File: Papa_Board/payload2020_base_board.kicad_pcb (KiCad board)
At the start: 4 copper layers, 82 x 82 mm, 101 parts, among them J1 1862, J10 1862, J11 Conn_01x05, J2 Conn_01x05, J3 Conn_01x05_Female, J4 Conn_01x05, J5 M80-5000642, J6 M80-5000642, J7 1862, J8 693072010801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

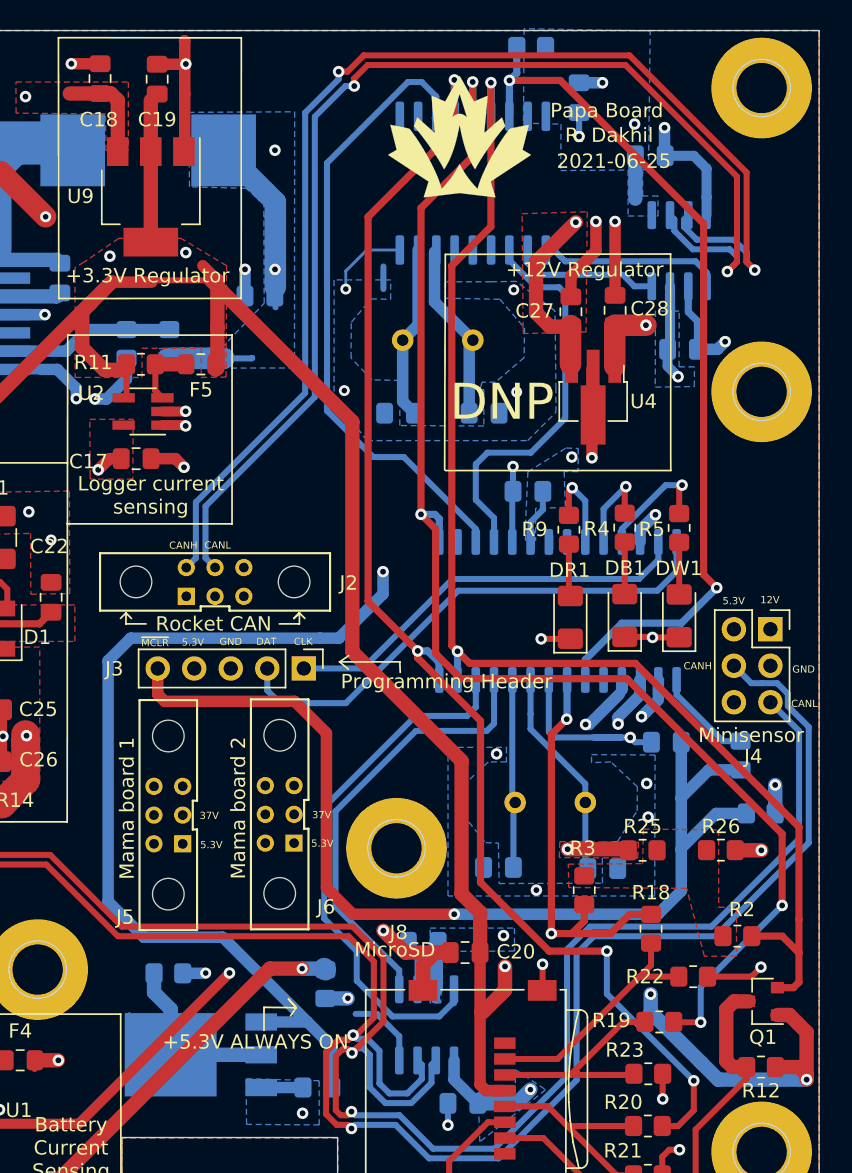
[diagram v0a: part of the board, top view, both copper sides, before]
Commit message: Move 3V3 line and rocket CAN traces
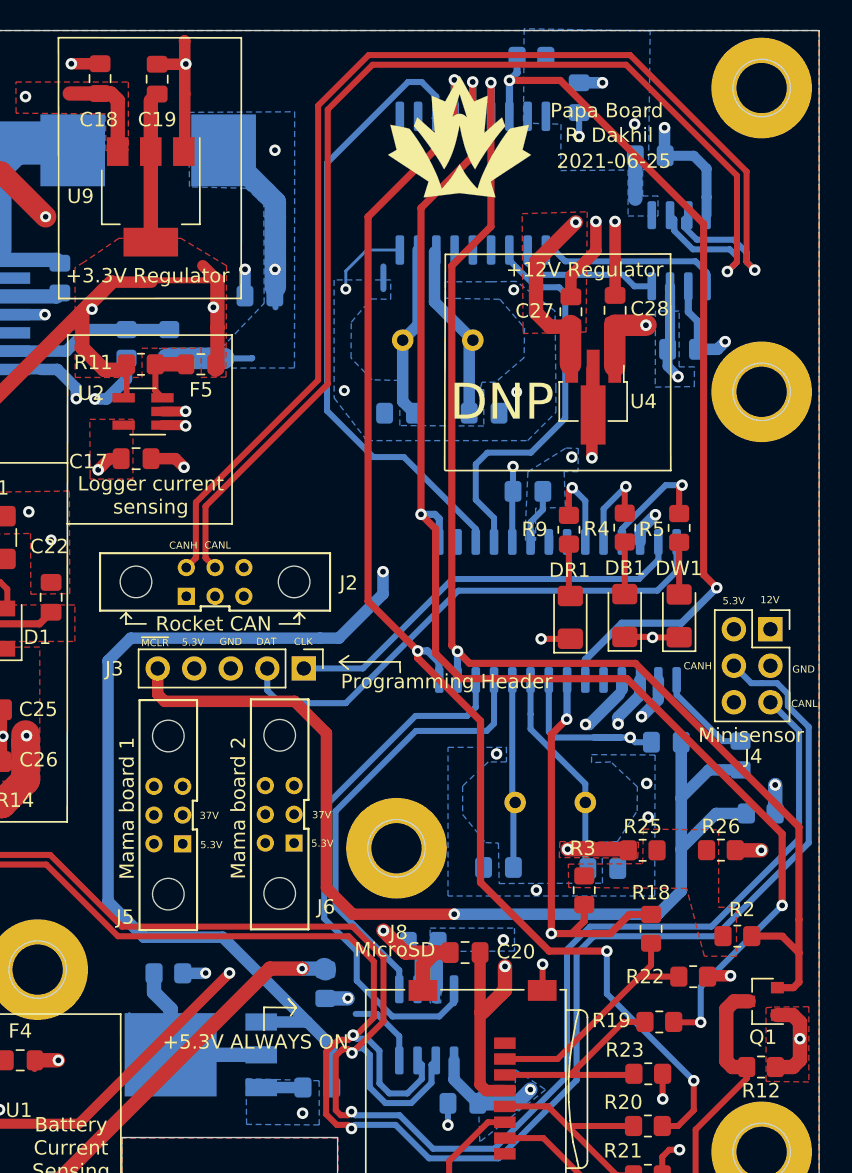
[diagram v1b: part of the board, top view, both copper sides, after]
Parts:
- moved R24 0.69 mm to (97.5, 69.1)
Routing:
- net +3V3: track 176.1 -> 189.5 mm, vias 5 -> 4
- net GND: track 182.9 -> 180.6 mm
- net /MCU and CAN controllers/CS_1: track 61.6 -> 60.8 mm
- net /CANL_ROCKET: track 83.7 -> 83.2 mm, vias 2 -> 1
- net /CANH_ROCKET: track 85.6 -> 85.1 mm, vias 2 -> 1

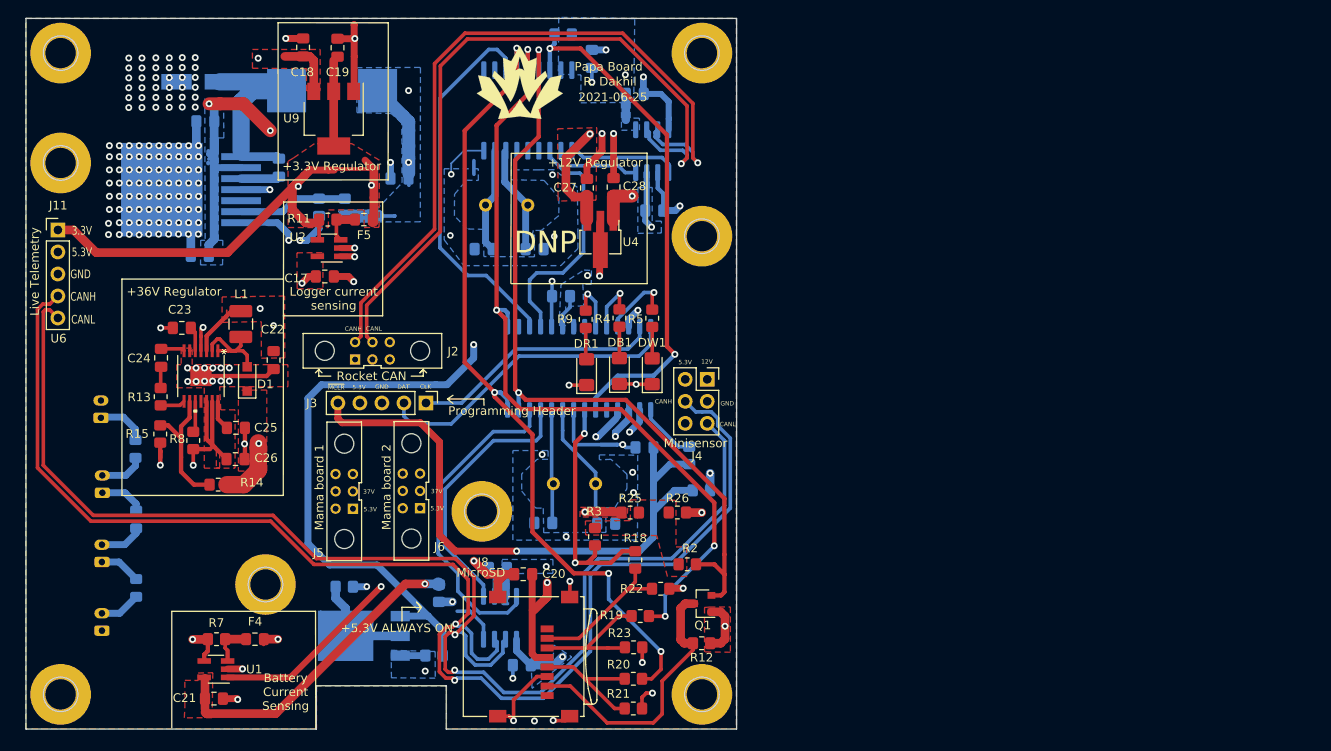
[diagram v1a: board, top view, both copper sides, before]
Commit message: Address Lance's comments, change microSD voltage divider resistor values (in-stock resistors)
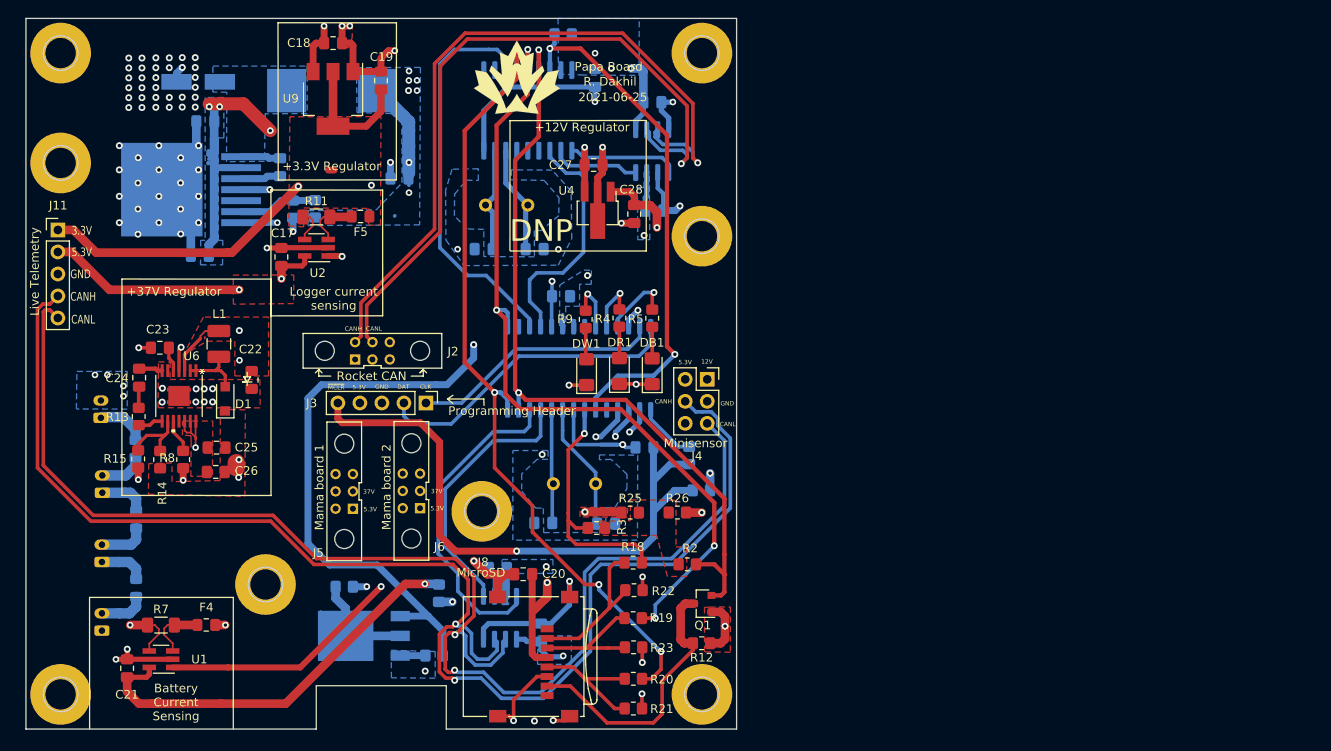
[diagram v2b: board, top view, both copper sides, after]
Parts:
- C7: value 56uF -> 100uF
- R11, R7: footprint Resistor_SMD:R_0805_2012Metric_Pad1.20x1.40mm_HandSolder -> Resistor_SMD:R_1206_3216Metric_Pad1.30x1.75mm_HandSolder
- R18, R19, R20: value 34kR -> 68kR
- R21, R22, R23: value 66kR -> 132kR
- moved C21 10.6 mm to (47.2, 142.3), turned to 270 degrees
- moved R14 7.30 mm to (51.0, 118.2), turned to 90 degrees
- moved R7 6.61 mm to (51.1, 137.3)
- moved U1 6.44 mm to (51.1, 141.3)
- moved C19 6.29 mm to (76.5, 74.5)
- moved F4 5.85 mm to (56.4, 137.3)
- moved C17 5.50 mm to (65.0, 94.8), turned to 270 degrees
- moved C14 4.36 mm to (95.0, 138.2), turned to 90 degrees
- moved C28 3.92 mm to (105.7, 89.9), turned to 270 degrees
- moved R15 3.84 mm to (48.5, 118.1)
- moved C18 3.50 mm to (71.0, 70.2), turned to 180 degrees
- moved R16 3.44 mm to (68.9, 89.3)
- moved D1 3.41 mm to (58.6, 111.2)
- moved C24 3.41 mm to (48.6, 108.8)
- moved R13 3.41 mm to (48.6, 113.2)
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- renumbered DW1 to DB1, DB1 to DR1, DR1 to DW1
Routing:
- net /+5.3V: track 72.8 -> 98.4 mm, vias 6 -> 12
- net Net-(C6-Pad1): track 25.4 -> 7.40 mm
- net +3V3: track 189.5 -> 172.6 mm
- net /+37V: track 11.5 -> 0.95 mm
- net Net-(R14-Pad2): track 15.5 -> 7.99 mm
- net GND: track 180.6 -> 173.5 mm, vias 168 -> 94
- net BATT_CURR_AMP: track 67.1 -> 73.0 mm
- net +BATT: track 105.4 -> 99.8 mm, vias 7 -> 12
- net /PWR_EN: track 81.4 -> 86.8 mm
- net Net-(R16-Pad2): track 12.6 -> 9.09 mm
- net Net-(D1-Pad2): track 11.5 -> 8.27 mm
- net /MCU and CAN controllers/CAN_INT: track 43.8 -> 46.1 mm
- net Net-(F4-Pad2): track 5.04 -> 7.06 mm
- net Net-(F5-Pad2): track 4.68 -> 6.41 mm
- net /5V3_ALWAYS_ON: track 33.4 -> 31.7 mm, vias 10 -> 11
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- added copper zone on B.Cu, net Net-(C6-Pad1)
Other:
- board text added: "+37V Regulator"
- board text removed: "+36V Regulator"

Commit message: Clean up via placement, SPI lines, polygons
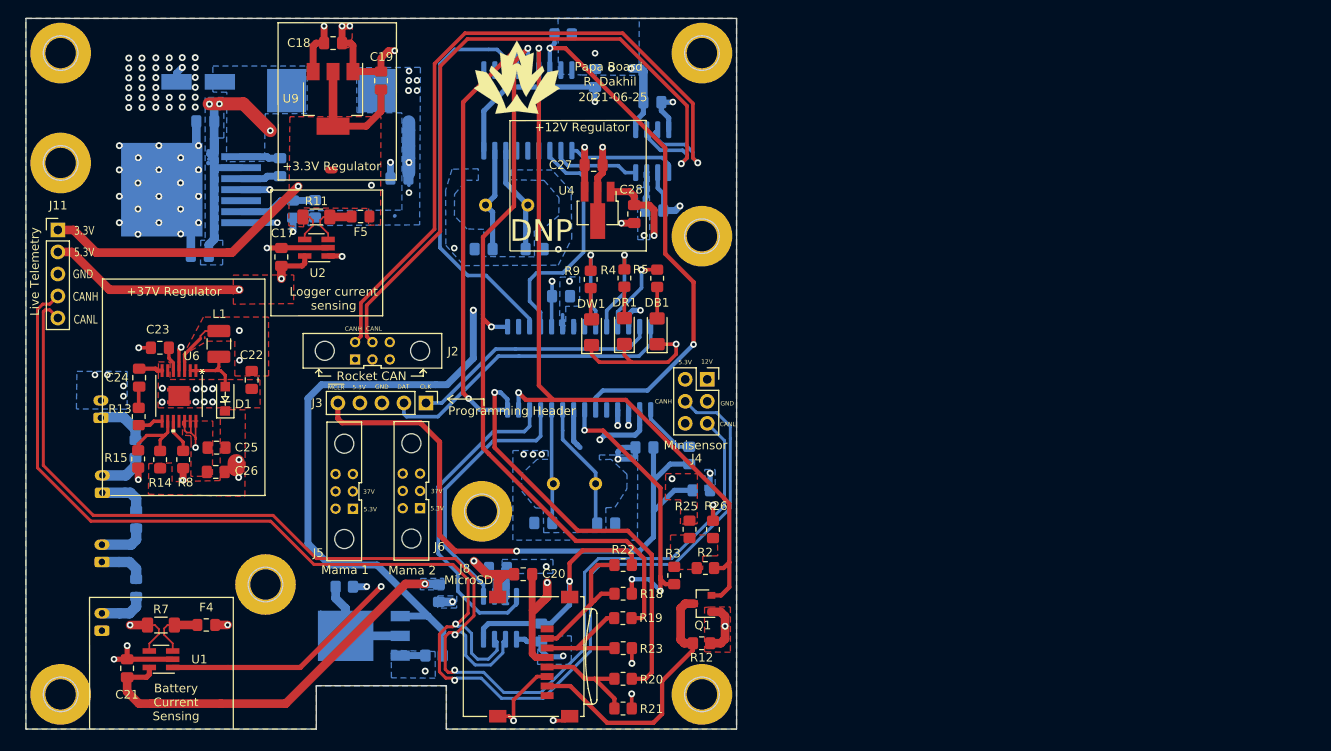
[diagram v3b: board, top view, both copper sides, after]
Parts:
- moved R3 10.5 mm to (110.4, 131.6), turned to 270 degrees
- moved R25 7.11 mm to (112.1, 126.3), turned to 270 degrees
- moved DB1 4.65 mm to (108.4, 103.4)
- moved DR1 4.65 mm to (104.6, 103.4)
- moved DW1 4.65 mm to (100.8, 103.5)
- moved R4 4.65 mm to (104.6, 97.3)
- moved R5 4.65 mm to (108.4, 97.3)
- moved R9 4.65 mm to (100.7, 97.4)
- moved R26 4.55 mm to (114.8, 126.3), turned to 90 degrees
- moved R18 3.77 mm to (104.5, 133.7)
- moved R22 3.16 mm to (104.5, 130.4)
- moved R2 2.14 mm to (114.0, 130.7)
- moved R23 1.20 mm to (104.5, 140.0)
- moved R19 1.19 mm to (104.4, 136.5)
- moved R20 1.19 mm to (104.5, 143.5)
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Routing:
- net GND: track 173.5 -> 195.5 mm
- net /+5.3V: track 98.4 -> 89.1 mm
- net /Logger board/MOSI: track 94.1 -> 86.5 mm, vias 4 -> 2
- net /Logger board/SCK: track 93.2 -> 100.2 mm, vias 4 -> 3
- net Net-(R4-Pad1): track 6.41 -> 10.8 mm
- net Net-(R9-Pad1): track 6.17 -> 10.3 mm
- net MAMA_PWR_EN: track 88.1 -> 91.8 mm
- net Net-(J8-Pad5): track 15.7 -> 12.7 mm
- net /Logger board/CS: track 31.0 -> 33.2 mm, vias 1 -> 3
- net Net-(J8-Pad3): track 15.7 -> 13.5 mm
- net 3V3_CURR_AMP: track 60.6 -> 58.7 mm
- net Net-(J8-Pad2): track 18.4 -> 16.7 mm
- net BATT_CURR_AMP: track 73.0 -> 71.4 mm
- net /MCU and CAN controllers/CS_1: track 60.8 -> 62.2 mm
- net /PWR_EN: track 86.8 -> 85.6 mm
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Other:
- net class Default: clearance 0.1524 -> 0.2032
- net class net removed
- rule trace_clearance: 0.1524 -> 0.2032
- board text added: "Mama 1"
- board text added: "Mama 2"
- board text removed: "Mama board 1"
- board text removed: "Mama board 2"

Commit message: Update D2 values and part number, update 10u capacitors' footprint
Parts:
- C22, C25, C26: footprint Capacitor_SMD:C_0805_2012Metric_Pad1.18x1.45mm_HandSolder -> Capacitor_SMD:C_1206_3216Metric_Pad1.33x1.80mm_HandSolder
- D2: value 500mV 2A -> 450mV 2A
- moved C22 0.67 mm to (61.6, 108.4)
- moved C26 0.39 mm to (57.7, 119.3)
- moved C25 0.30 mm to (57.8, 116.7)
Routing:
- net /+37V: track 0.95 -> 0.37 mm, vias 2 -> 3
- net +BATT: vias 12 -> 13
